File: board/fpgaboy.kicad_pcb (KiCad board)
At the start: 4 copper layers, 50 x 50 mm, 87 parts, among them J1 Conn_01x12, J2 Conn_01x06, J3 Micro_SD_Card_Det, J4 Conn_01x06, P1 ILI9341, P2 CONN_01X02, P3 USB_OTG, Q1 BSS816NW, SW1 SWITCH_SPST, U1 iCE40-HX8k-BG121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

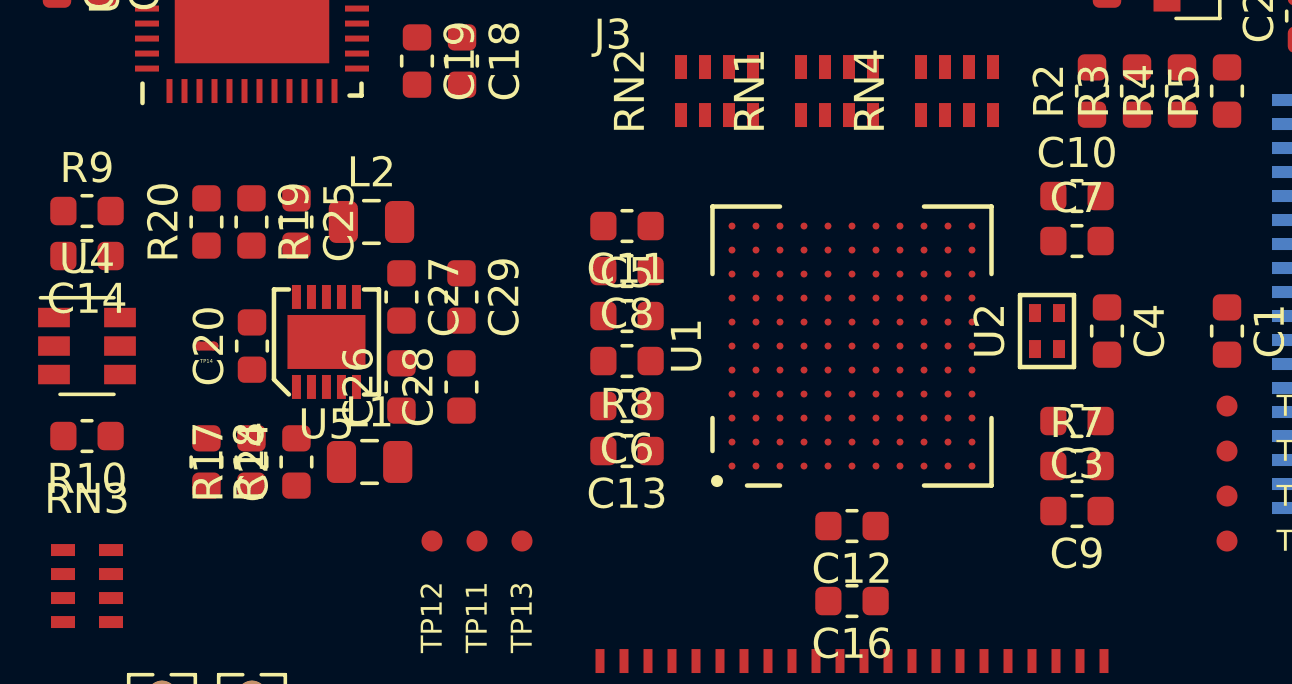
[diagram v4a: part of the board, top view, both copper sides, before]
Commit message: kicad crashed and deleted all traces from the board. wtf? 3 hours' progress lost. Only some vias under the BGA are left. Should commit more often
Former-commit-id: 02cf3a33ecf67da1eb78e7c40696abeefd4b2115 [formerly 0f2dd3bf6e83a96bdb5da01df3e7540a826b344c]
Former-commit-id: e1ce6b3b8ad0493b9ac25c1ada88c924ade3c314
Former-commit-id: 9ae19f32a7b680d308611b0b1fcd16b73eed0f11
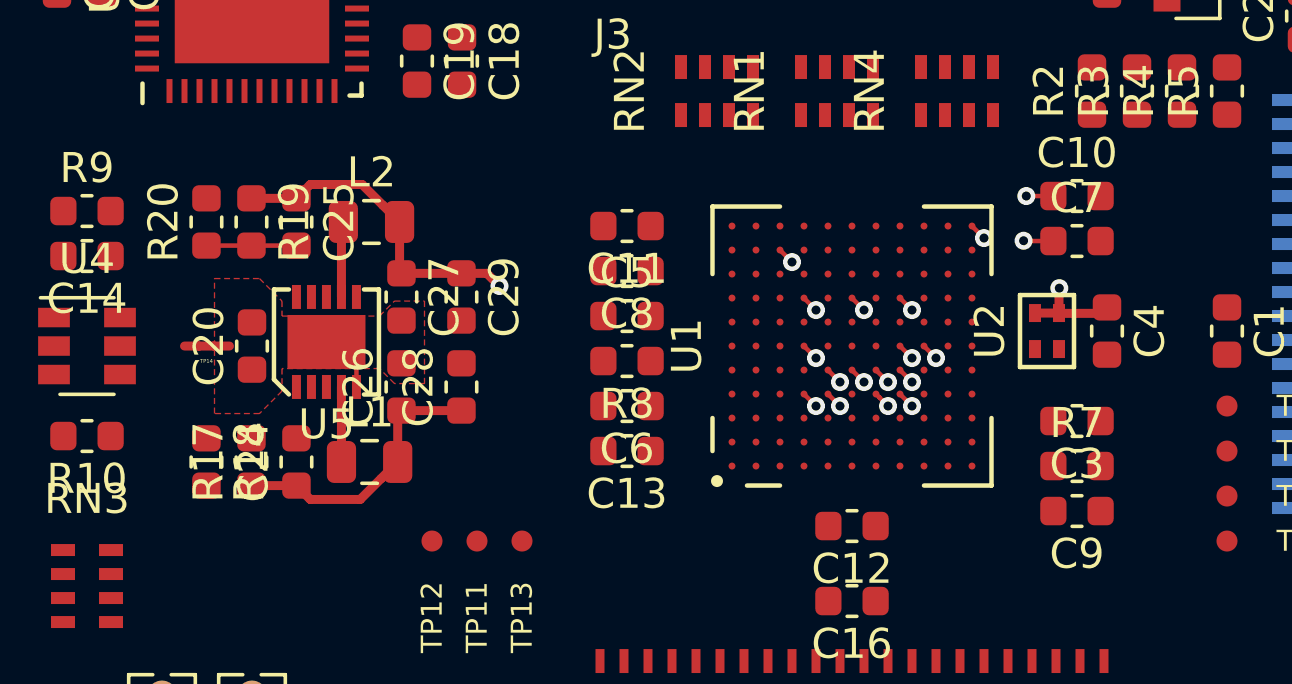
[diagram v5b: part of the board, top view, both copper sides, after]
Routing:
- net +3V3: track 0.00 -> 17.5 mm, vias 0 -> 9
- net +1V2: track 0.00 -> 14.1 mm, vias 0 -> 6
- net Net-(C25-Pad2): track 0.00 -> 3.00 mm
- net GND: track 0.00 -> 2.75 mm, vias 0 -> 4
- net GNDPWR: track 0.00 -> 2.64 mm
- net Net-(L2-Pad1): track 0.00 -> 2.53 mm
- net Net-(L1-Pad1): track 0.00 -> 2.50 mm
- net /VCCPLL0: track 0.00 -> 0.57 mm, vias 0 -> 1
- added copper zone on F.Cu, net GNDPWR

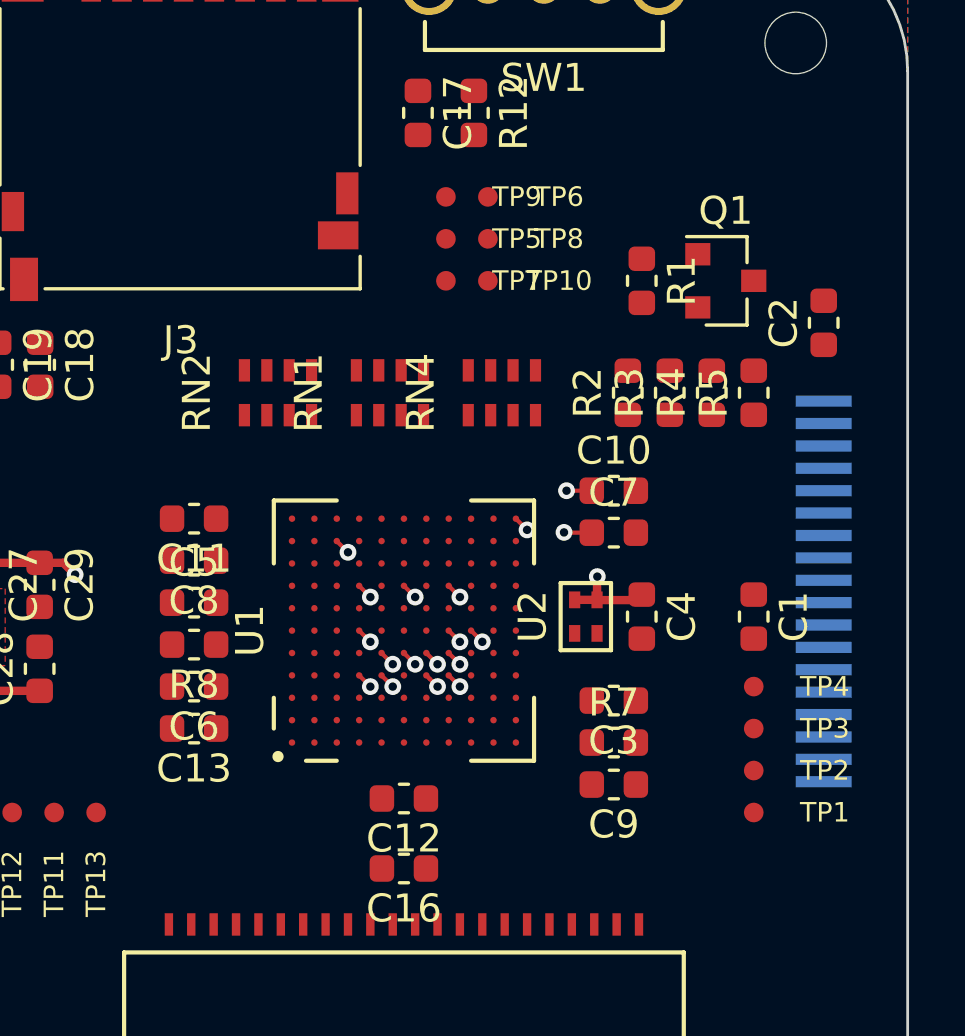
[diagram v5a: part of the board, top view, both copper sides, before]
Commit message: Add extra zones under BGA to tighten up plane clearance (so that planes can go between diagonally-spaced vias).
Former-commit-id: acc1dc0282ce864e70f9f44a6a4090a0b3997665 [formerly ad3864c5784006ca55ec16fa14b2cfcdcb240494]
Former-commit-id: f4db6870202bdf4893f368656aa2d5cde32939b2
Former-commit-id: 2560b549215e1b4d3805b382c28499008ce62867
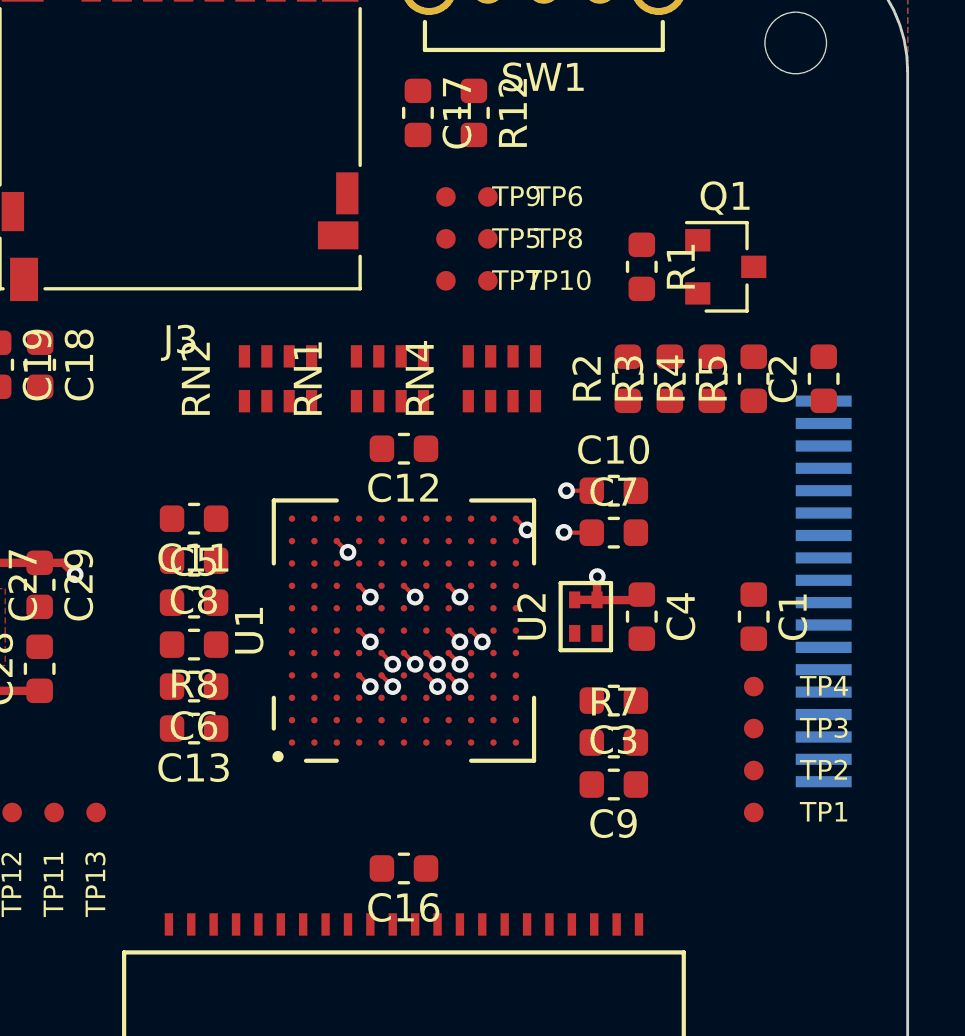
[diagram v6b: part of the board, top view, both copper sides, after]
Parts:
- moved C12 12.5 mm to (162.0, 98.5)
- moved C2 2.00 mm to (177.0, 96.0)
- moved Q1 0.50 mm to (173.5, 92.0)
- moved R1 0.50 mm to (170.5, 92.0)
- moved R2 0.50 mm to (170.0, 96.0)
- moved R3 0.50 mm to (171.5, 96.0)
- moved R4 0.50 mm to (173.0, 96.0)
- moved R5 0.50 mm to (174.5, 96.0)
- moved RN1 0.50 mm to (161.5, 96.0)
- moved RN2 0.50 mm to (157.5, 96.0)
- moved RN4 0.50 mm to (165.5, 96.0)
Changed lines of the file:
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@@
   (page A4)
   (layers
-    (0 F.Cu signal hide)
-    (1 In1.Cu power hide)
+    (0 F.Cu signal)
+    (1 In1.Cu power)
     (2 In2.Cu power)
     (31 B.Cu signal)
@@
   )
   (setup
-    (last_trace_width 1.5)
+    (last_trace_width 0.15)
     (user_trace_width 0.2)
     (user_trace_width 0.3)
@@
   )
   (module Capacitor_SMD:C_0603_1608Metric (layer F.Cu)
-    (at 177 94 90)
+    (at 177 96 90)
     (descr "Capacitor SMD 0603 (1608 Metric), square (rectangular) end terminal, IPC_7351 nominal, (Body size source: http://www.tortai-tech.com/upload/download/2011102023233369053.pdf), generated with kicad-footprint-generator")
     (tags capacitor)
@@
   )
   (module Capacitor_SMD:C_0603_1608Metric (layer F.Cu)
-    (at 162 111 180)
+    (at 162 98.5 180)
     (descr "Capacitor SMD 0603 (1608 Metric), square (rectangular) end terminal, IPC_7351 nominal, (Body size source: http://www.tortai-tech.com/upload/download/2011102023233369053.pdf), generated with kicad-footprint-generator")
     (tags capacitor)
@@
   )
   (module fpgaboy_parts:RN4-1206 (layer F.Cu)
-    (at 161.5 96.5)
+    (at 161.5 96)
     (attr smd)
     (fp_text reference RN1 (at -2.9 0 90) (layer F.SilkS)
@@
   )
   (module fpgaboy_parts:RN4-1206 (layer F.Cu)
-    (at 157.5 96.5)
+    (at 157.5 96)
     (attr smd)
     (fp_text reference RN2 (at -2.9 0 90) (layer F.SilkS)
@@
   )
   (module fpgaboy_parts:RN4-1206 (layer F.Cu)
-    (at 165.5 96.5)
+    (at 165.5 96)
     (attr smd)
     (fp_text reference RN4 (at -2.9 0 90) (layer F.SilkS)
@@
   )
   (module Resistor_SMD:R_0603_1608Metric (layer F.Cu)
-    (at 170.5 92.5 270)
+    (at 170.5 92 270)
     (descr "Resistor SMD 0603 (1608 Metric), square (rectangular) end terminal, IPC_7351 nominal, (Body size source: http://www.tortai-tech.com/upload/download/2011102023233369053.pdf), generated with kicad-footprint-generator")
     (tags resistor)
@@
   )
   (module Resistor_SMD:R_0603_1608Metric (layer F.Cu)
-    (at 170 96.5 90)
+    (at 170 96 90)
     (descr "Resistor SMD 0603 (1608 Metric), square (rectangular) end terminal, IPC_7351 nominal, (Body size source: http://www.tortai-tech.com/upload/download/2011102023233369053.pdf), generated with kicad-footprint-generator")
     (tags resistor)
@@
   )
   (module Resistor_SMD:R_0603_1608Metric (layer F.Cu)
-    (at 171.5 96.5 90)
+    (at 171.5 96 90)
     (descr "Resistor SMD 0603 (1608 Metric), square (rectangular) end terminal, IPC_7351 nominal, (Body size source: http://www.tortai-tech.com/upload/download/2011102023233369053.pdf), generated with kicad-footprint-generator")
     (tags resistor)
@@
   )
   (module Resistor_SMD:R_0603_1608Metric (layer F.Cu)
-    (at 173 96.5 90)
+    (at 173 96 90)
     (descr "Resistor SMD 0603 (1608 Metric), square (rectangular) end terminal, IPC_7351 nominal, (Body size source: http://www.tortai-tech.com/upload/download/2011102023233369053.pdf), generated with kicad-footprint-generator")
     (tags resistor)
@@
   )
   (module Resistor_SMD:R_0603_1608Metric (layer F.Cu)
-    (at 174.5 96.5 90)
+    (at 174.5 96 90)
     (descr "Resistor SMD 0603 (1608 Metric), square (rectangular) end terminal, IPC_7351 nominal, (Body size source: http://www.tortai-tech.com/upload/download/2011102023233369053.pdf), generated with kicad-footprint-generator")
     (tags resistor)
@@
   )
   (module Package_TO_SOT_SMD:SOT-23 (layer F.Cu)
-    (at 173.5 92.5)
+    (at 173.5 92)
     (descr "SOT-23, Standard")
     (tags SOT-23)
@@
       )
     )
+  )
+  (zone (net 1) (net_name GND) (layer In1.Cu) (hatch edge 0.508)
+    (priority 1)
+    (connect_pads yes (clearance 0.15))
+    (min_thickness 0.15)
+    (fill (arc_segments 16) (thermal_gap 0.508) (thermal_bridge_width 0.508))
+    (polygon
+      (pts
+        (xy 156 99) (xy 168 99) (xy 168 111.5) (xy 156 111.5)
+      )
+    )
+  )
+  (zone (net 2) (net_name +3V3) (layer In2.Cu) (hatch edge 0.508)
+    (priority 1)
+    (connect_pads (clearance 0.15))
+    (min_thickness 0.15)
+    (fill (arc_segments 16) (thermal_gap 0.508) (thermal_bridge_width 0.508))
+    (polygon
+      (pts
+        (xy 155.5 98.5) (xy 168.5 98.5) (xy 168.5 112) (xy 155.5 112)
+      )
+    )
